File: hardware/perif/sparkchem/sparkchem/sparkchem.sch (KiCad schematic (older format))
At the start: 6 parts

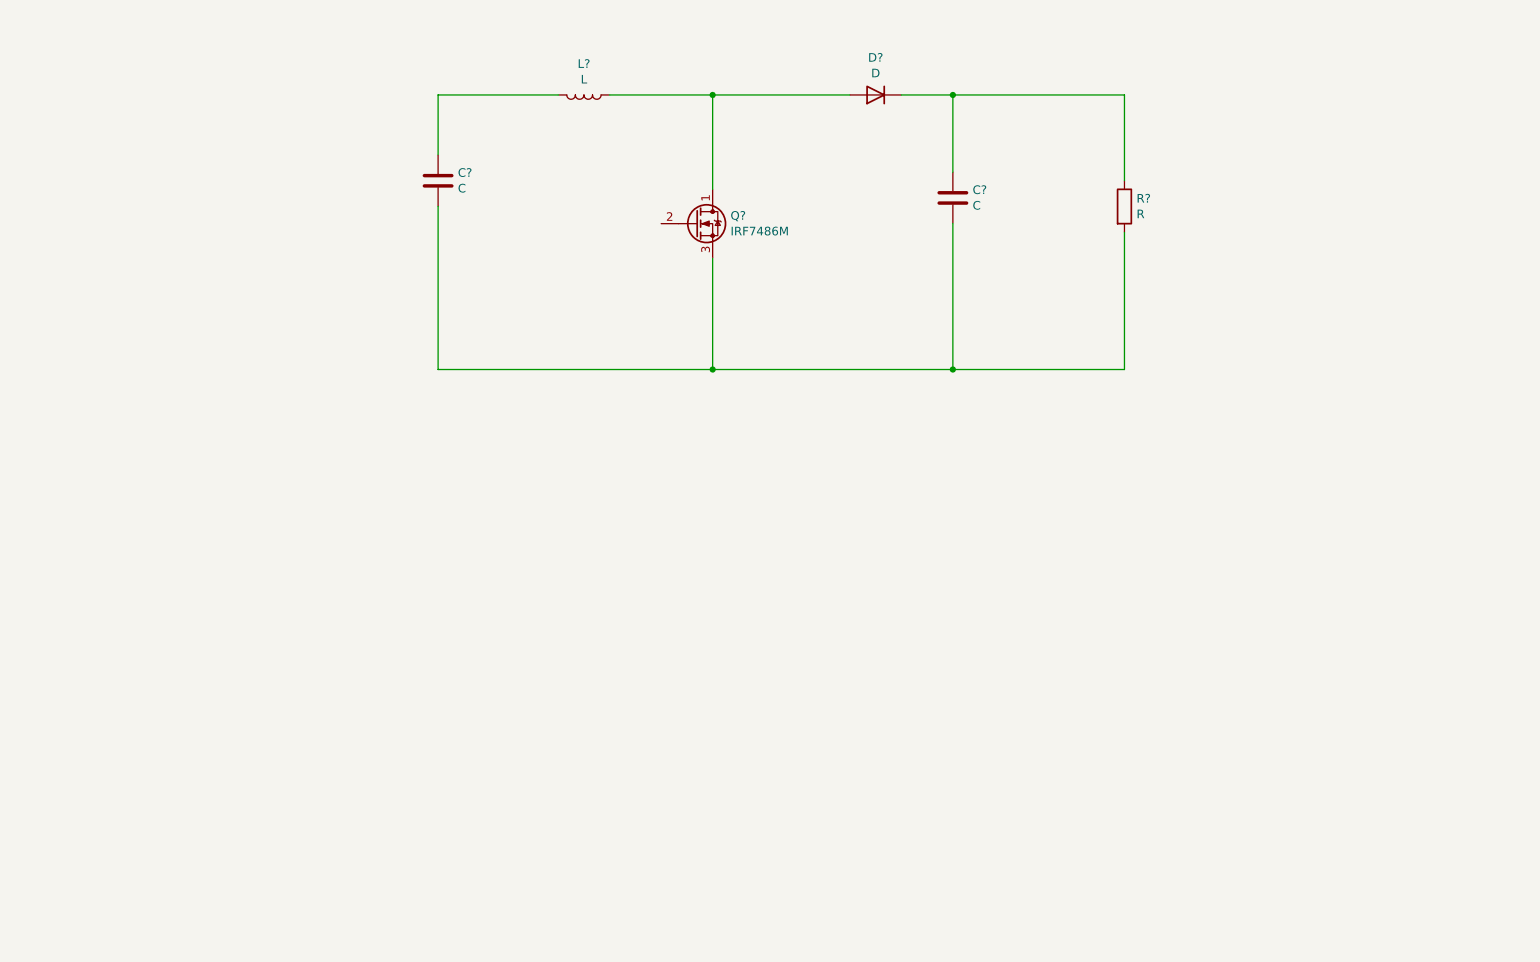
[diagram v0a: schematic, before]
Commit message: started u-blox GPS CAM-M8Q footpring and spark experiment
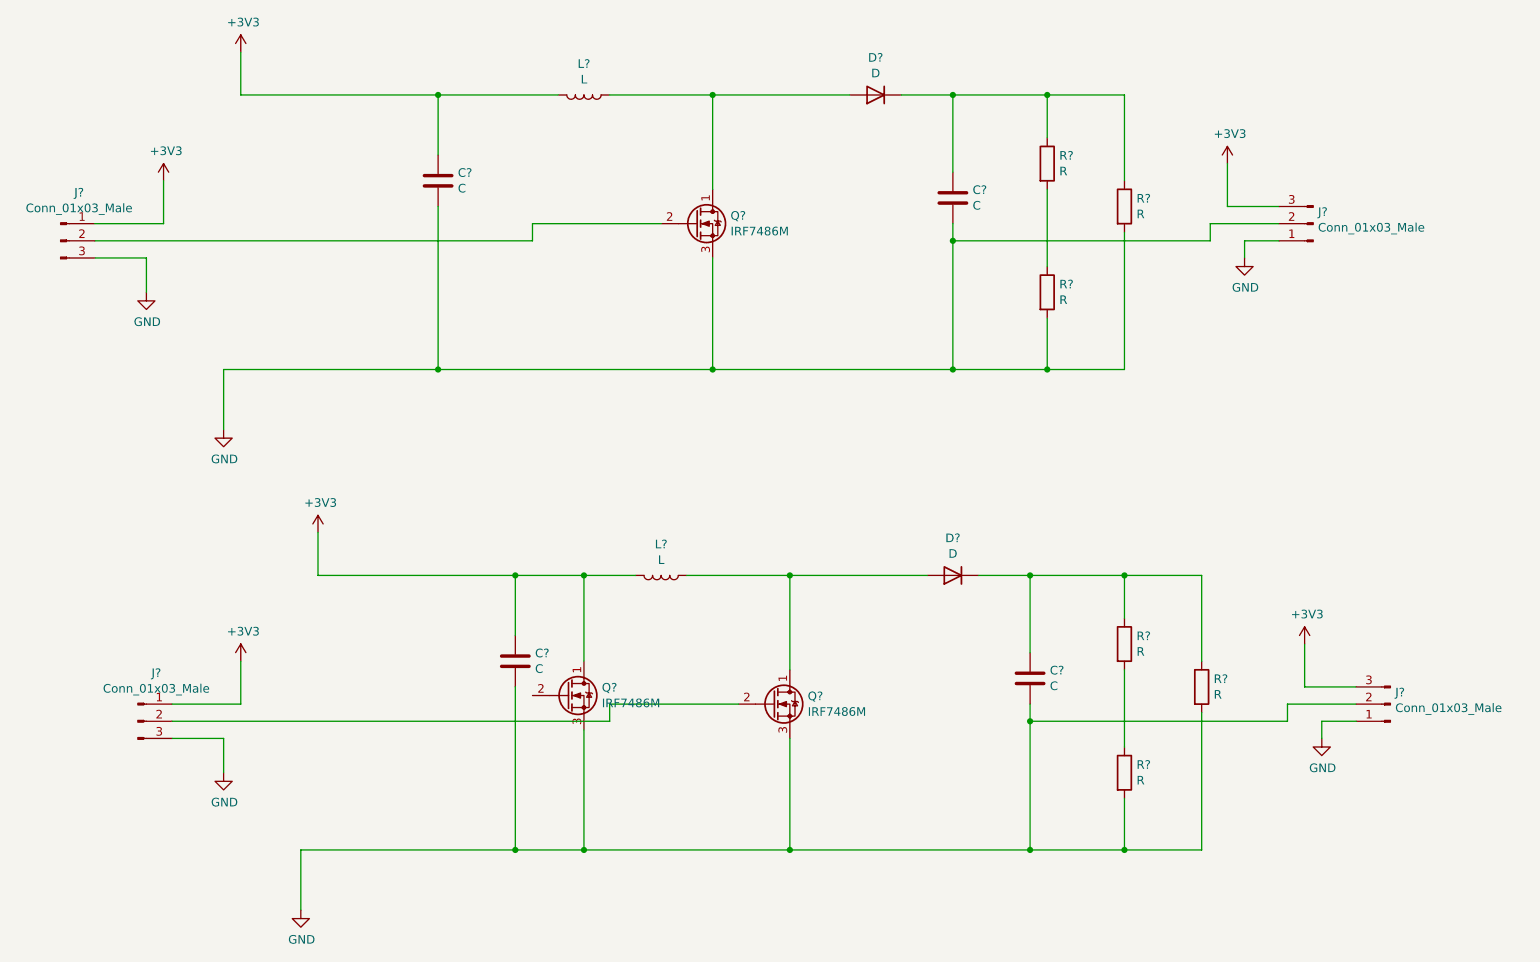
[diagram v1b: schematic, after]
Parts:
- added C? (x2): C, symbol Device:C
- added D?: D, symbol Device:D
- added J? (x4): Conn_01x03_Male, symbol Connector:Conn_01x03_Male
- added L?: L, symbol Device:L
- added Q? (x2): IRF7486M, Package_DirectFET:DirectFET_ME, symbol Transistor_FET:IRF7486M
- added R? (x5): R, symbol Device:R
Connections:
- net at Q?.2 (G): now also J?.2 (Pin_2)
- net GND: now reaches C?.2, C?.2, Q?.3 (S), R?.2
- net GND: now also C?.2, C?.2, J?.1 (Pin_1), J?.1 (Pin_1), J?.2 (Pin_2), J?.2 (Pin_2), J?.3 (Pin_3), J?.3 (Pin_3), Q?.3 (S), Q?.3 (S), R?.2, R?.2, R?.2
- net at C?.1, D?.1 (K), R?.1: now also R?.1
- net +3V3: now reaches C?.1, L?.2
- net +3V3: now also C?.1, J?.1 (Pin_1), J?.1 (Pin_1), J?.3 (Pin_3), J?.3 (Pin_3), L?.2, Q?.1 (D)
- new net: R?.1, R?.2 (x2)
- new net: D?.2 (A), L?.1, Q?.1 (D)
- new net: J?.2 (Pin_2), Q?.2 (G)
- new net: C?.1, D?.1 (K), R?.1, R?.1

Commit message: periferals
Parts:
- removed C? (x4): C, symbol Device:C
- removed D? (x2): D, symbol Device:D
- removed J? (x4): Conn_01x03_Male, symbol Connector:Conn_01x03_Male
- removed L? (x2): L, symbol Device:L
- removed Q? (x3): IRF7486M, Package_DirectFET:DirectFET_ME, symbol Transistor_FET:IRF7486M
- removed R? (x6): R, symbol Device:R
